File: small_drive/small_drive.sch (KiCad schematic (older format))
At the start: 159 parts, among them J1 DB9, J2 DB15, M1 SiR826DP, M2 SiR826DP, M3 SiR826DP, M4 SiR826DP, M5 SiR826DP, M6 SiR826DP, P1 CONN_01X04, P2 CONN_01X04, P3 CONN_01X04, P4 CONN_01X04, P5 CONN_01X02, P6 CONN_01X02, P7 CONN_01X02, P8 CONN_01X01, U1 XMC4400-F64x512, U10 LM5106, U11 ACS711KLCTR-12AB-T, U12 ACS711ELCTR-25AB-T, U13 ACS711KLCTR-12AB-T, U14 AD8226, U15 MAX3096, U16 AMC1203, U17 7805, U18 LT1764EQ, U19 KSZ8081, U2 ips511g, U20 ETH100_MAG, U3 ips511g, U4 LTC2850, U5 AD8226, U6 LT1764EQ, U7 MC33074DTBR2, U8 LM5106, U9 LM5106, X1 NKE1212DC, X2 NKE1212DC, X3 HCPL0201, X4 HCPL0201, X5 HCPL0201, X6 HCPL0201, Y1 12MHz, Y2 25MHz

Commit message: Doesn't work. Clocks?
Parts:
- U11, U12, U13: Digikey 620-1371-1-ND -> 620-1370-1-ND
- U17: Farnell (none) -> 1102157
- Y1: Farnell (none) -> 2508630; Manufacturer (none) -> QANTEK TECHNOLOGY CORPORATION; PartNr (none) -> QC3CA12.0000F12B23M
- Y2: Farnell (none) -> 2508942; Manufacturer (none) -> QANTEK TECHNOLOGY CORPORATION; PartNr (none) -> QC3CA25.0000F18B23M
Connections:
- wire segments 900 -> 666

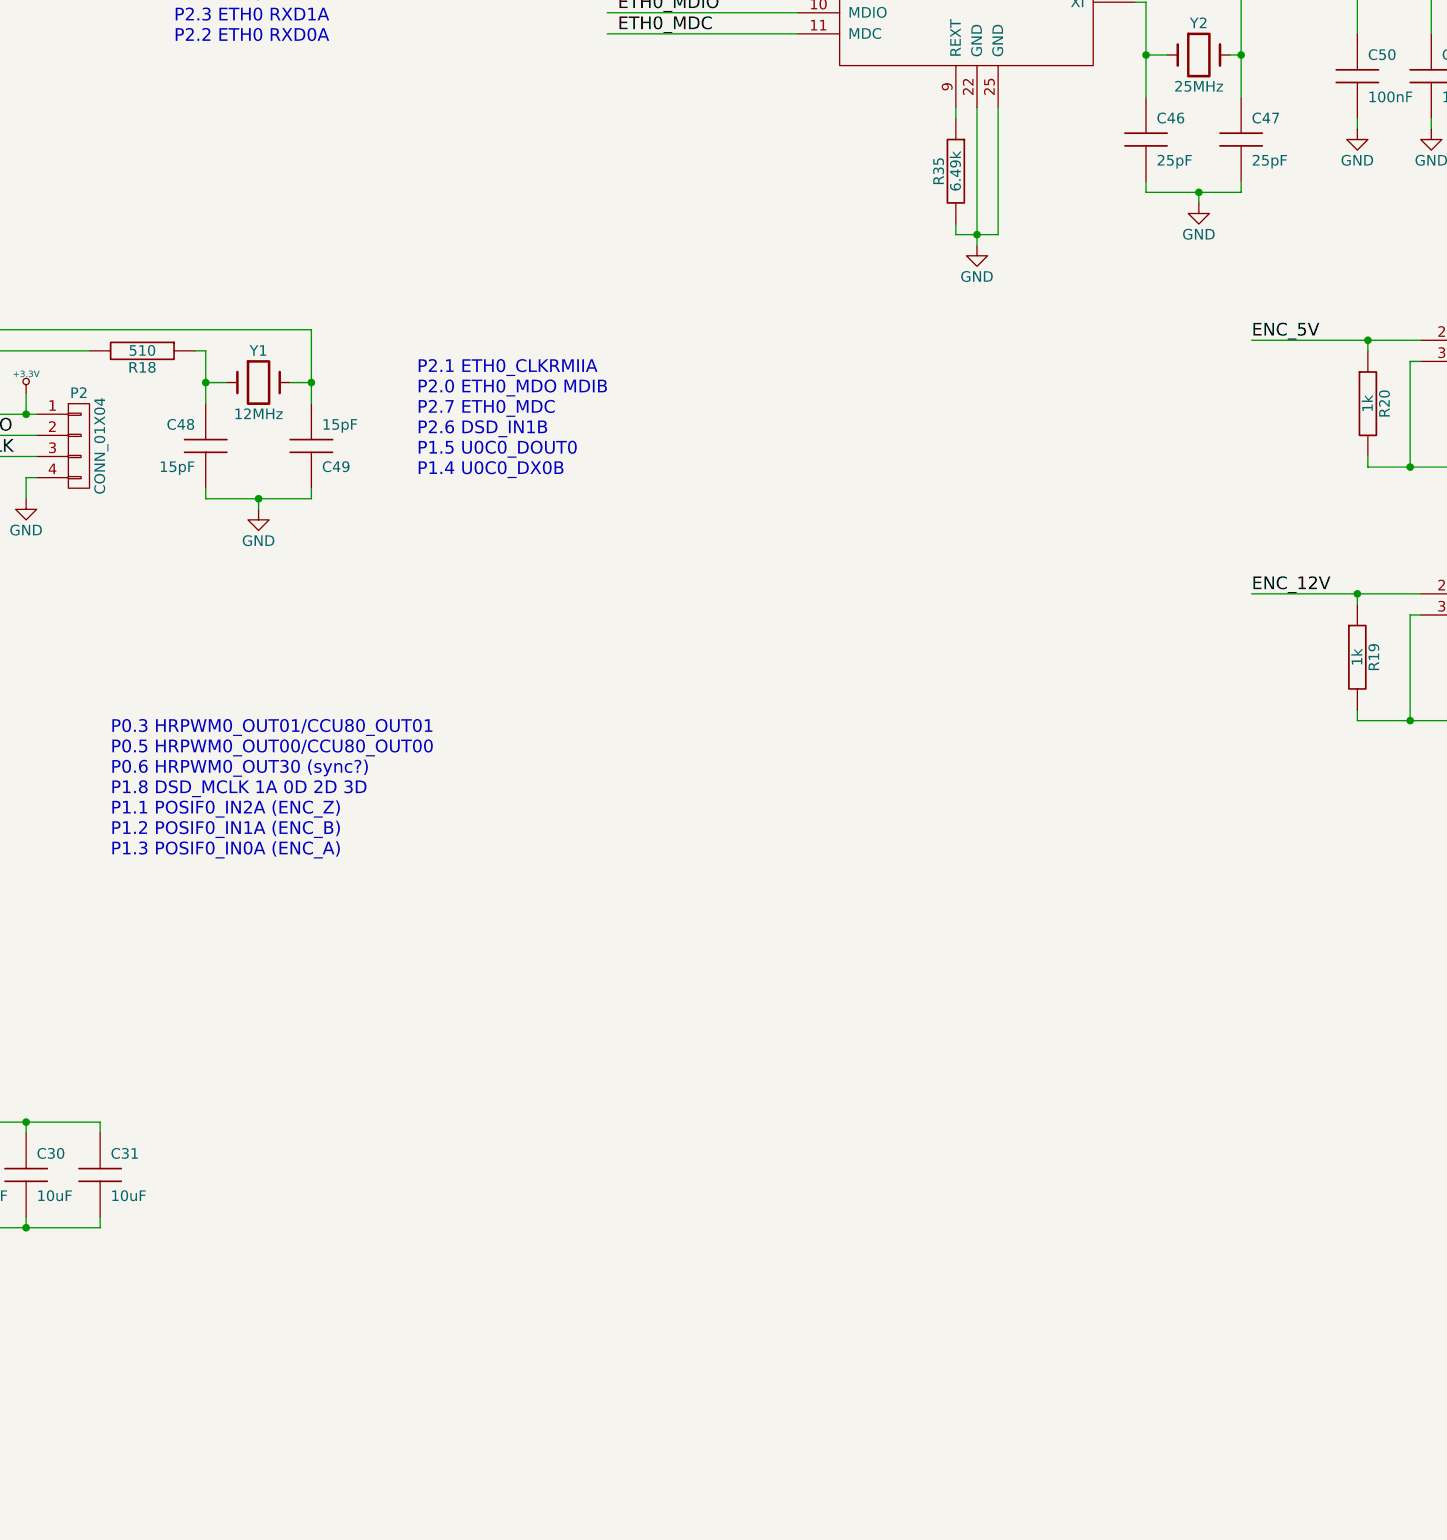
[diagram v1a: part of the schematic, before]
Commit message: Header conversion in C++
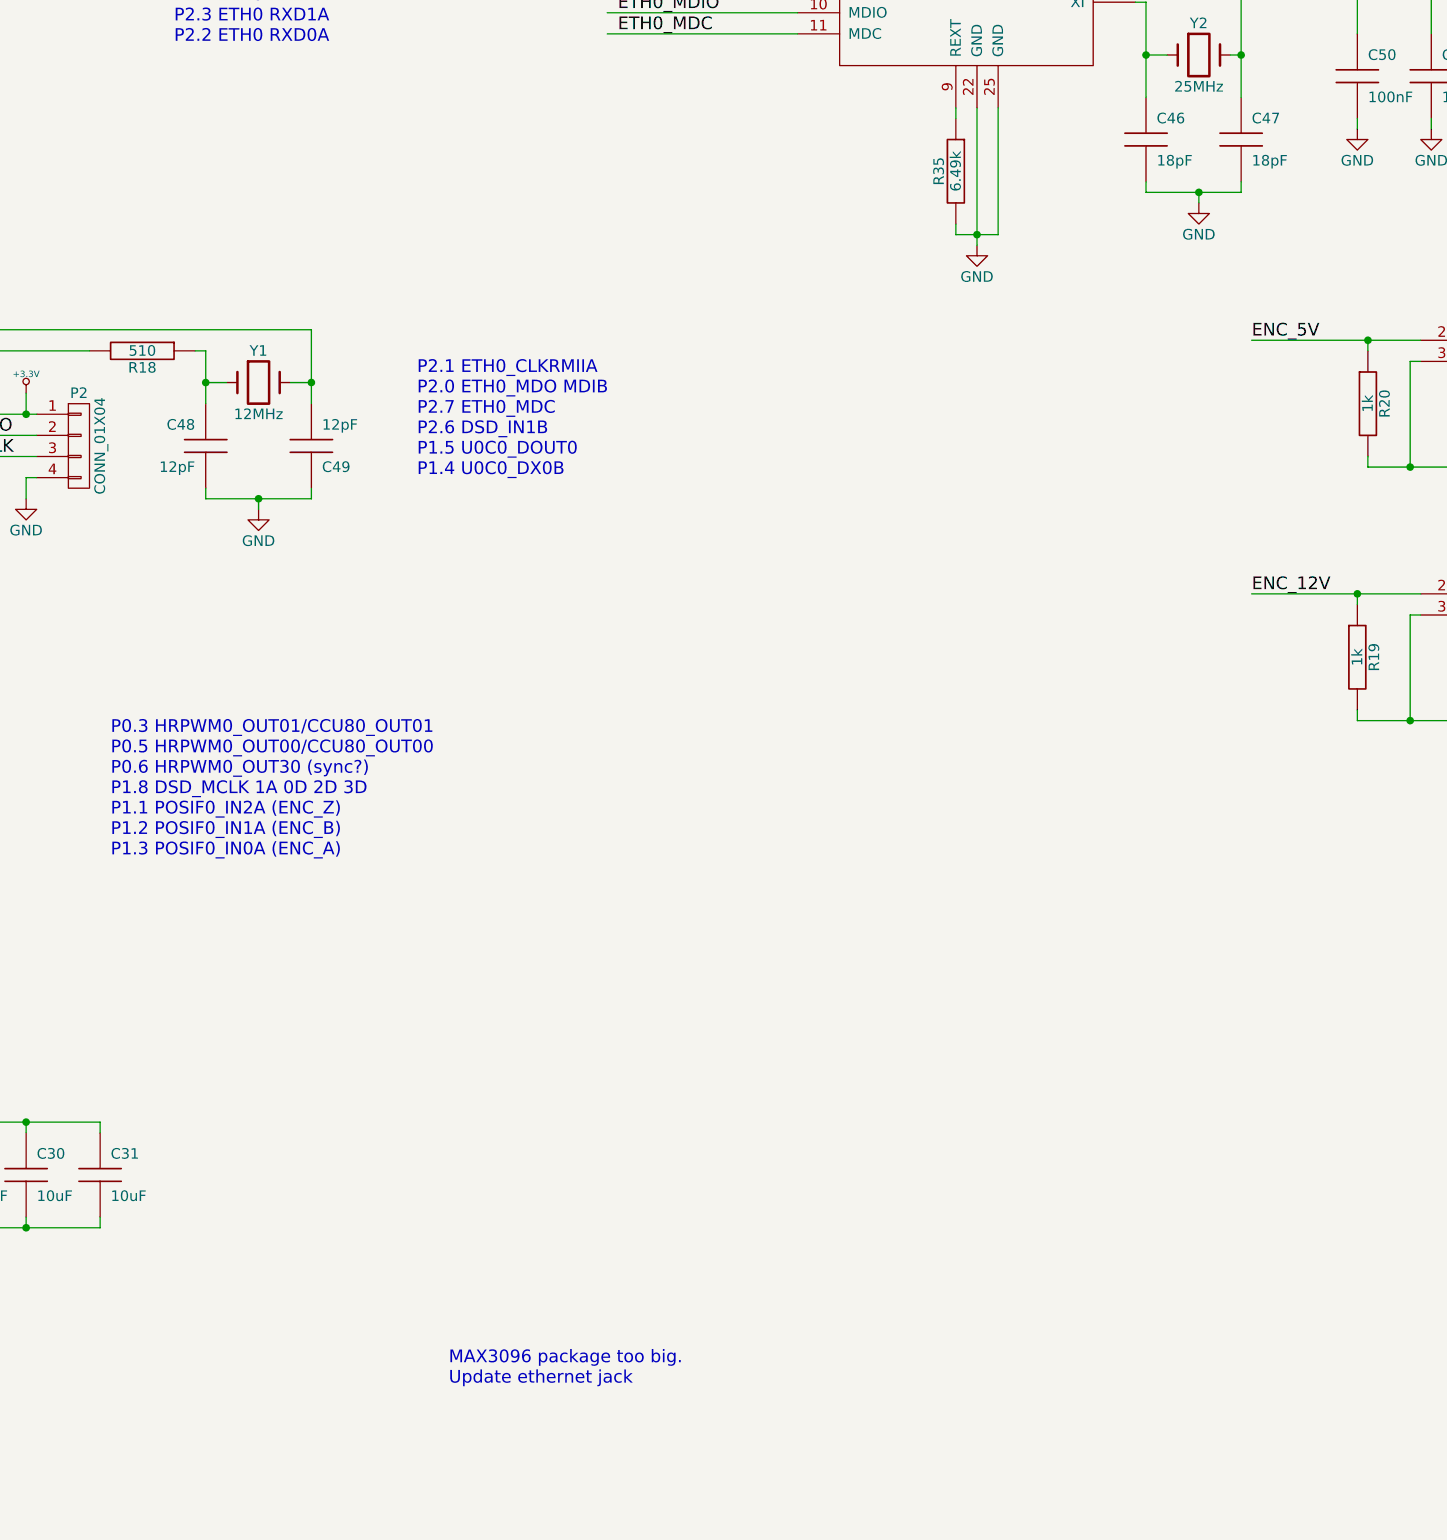
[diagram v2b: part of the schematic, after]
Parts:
- C46, C47: value 25pF -> 18pF
- C48, C49: value 15pF -> 12pF
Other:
- note added: "MAX3096 package too big.\nUpdate ethernet jack"
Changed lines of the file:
@@
 P 3800 9550
 F 0 "C48" H 3850 9650 50  0000 L CNN
-F 1 "15pF" H 3850 9450 50  0000 L CNN
+F 1 "12pF" H 3850 9450 50  0000 L CNN
 F 2 "Capacitors_SMD:C_0603" H 3800 9550 60  0001 C CNN
 F 3 "" H 3800 9550 60  0000 C CNN
@@
 P 4300 9550
 F 0 "C49" H 4350 9650 50  0000 L CNN
-F 1 "15pF" H 4350 9450 50  0000 L CNN
+F 1 "12pF" H 4350 9450 50  0000 L CNN
 F 2 "Capacitors_SMD:C_0603" H 4300 9550 60  0001 C CNN
 F 3 "" H 4300 9550 60  0000 C CNN
@@
 P 8250 8100
 F 0 "C46" H 8300 8200 50  0000 L CNN
-F 1 "25pF" H 8300 8000 50  0000 L CNN
+F 1 "18pF" H 8300 8000 50  0000 L CNN
 F 2 "Capacitors_SMD:C_0603" H 8250 8100 60  0001 C CNN
 F 3 "" H 8250 8100 60  0000 C CNN
@@
 P 8700 8100
 F 0 "C47" H 8750 8200 50  0000 L CNN
-F 1 "25pF" H 8750 8000 50  0000 L CNN
+F 1 "18pF" H 8750 8000 50  0000 L CNN
 F 2 "Capacitors_SMD:C_0603" H 8700 8100 60  0001 C CNN
 F 3 "" H 8700 8100 60  0000 C CNN
@@
 Text Label 2600 9600 0    60   ~ 0
 SWCLK
+Text Notes 4950 14000 0    60   ~ 0
+MAX3096 package too big.\nUpdate ethernet jack
 $EndSCHEMATC

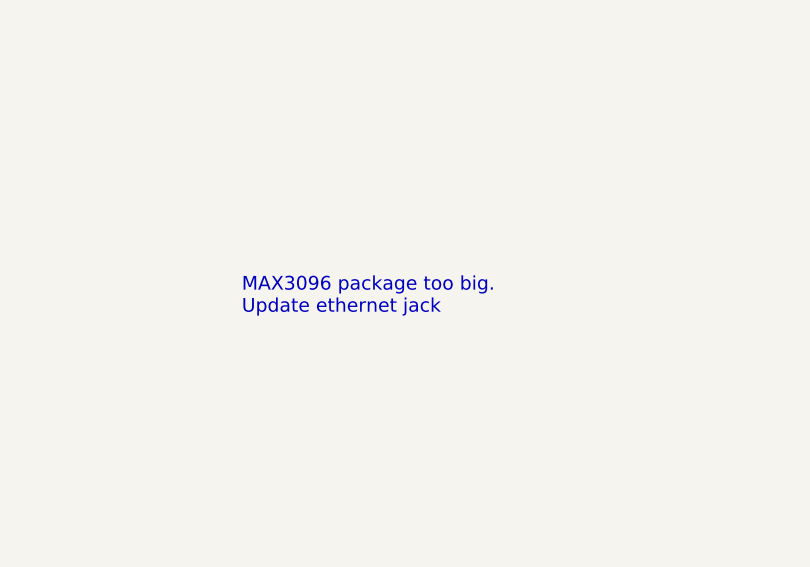
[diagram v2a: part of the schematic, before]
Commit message: Initial test on XMC4400, LED0/mdc/mdio works.
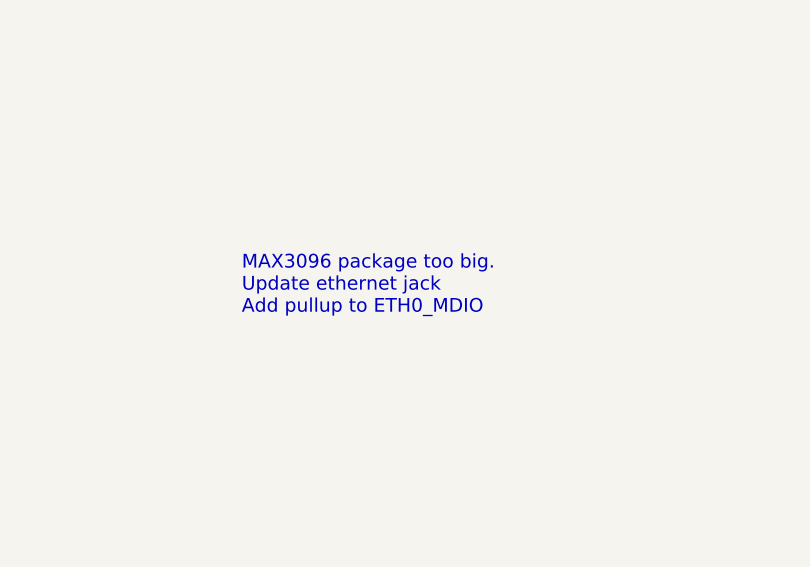
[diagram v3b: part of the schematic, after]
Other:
- note added: "MAX3096 package too big.\nUpdate ethernet jack\nAdd pullup to ETH0_MDIO"
- note removed: "MAX3096 package too big.\nUpdate ethernet jack"
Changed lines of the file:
@@
 SWCLK
 Text Notes 4950 14000 0    60   ~ 0
-MAX3096 package too big.\nUpdate ethernet jack
+MAX3096 package too big.\nUpdate ethernet jack\nAdd pullup to ETH0_MDIO
 $EndSCHEMATC

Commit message: PWM (low resolution) works.
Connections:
- wire segments 666 -> 901
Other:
- note added: "P1.3 POSIF0 IN0A\nP1.2 POSIF0 IN1A\nP1.1 POSIF0 IN2A\nP1.8 DSD MCLK1\nP0.6 HRPWM0 HROUT30\nP0.5 HRPWM0 HROUT00\nP0.3 HRPWM0 HROUT20"
- note removed: "P0.3 HRPWM0_OUT01/CCU80_OUT01\nP0.5 HRPWM0_OUT00/CCU80_OUT00\nP0.6 HRPWM0_OUT30 (sync?)\nP1.8 DSD_MCLK 1A 0D 2D 3D\nP1.1 POSIF0_IN2A (ENC_Z)\nP1.2 POSIF0_IN1A (ENC_B)\nP1.3 POSIF0_IN0A (ENC_A)"
